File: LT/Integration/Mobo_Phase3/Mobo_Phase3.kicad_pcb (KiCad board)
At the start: 4 copper layers, 90.2 x 95.9 mm, 39 parts, among them J1 Bus, J2 Conn_Coaxial, J6 Conn_Coaxial, Q1 2N5486, U1 BAP64Q

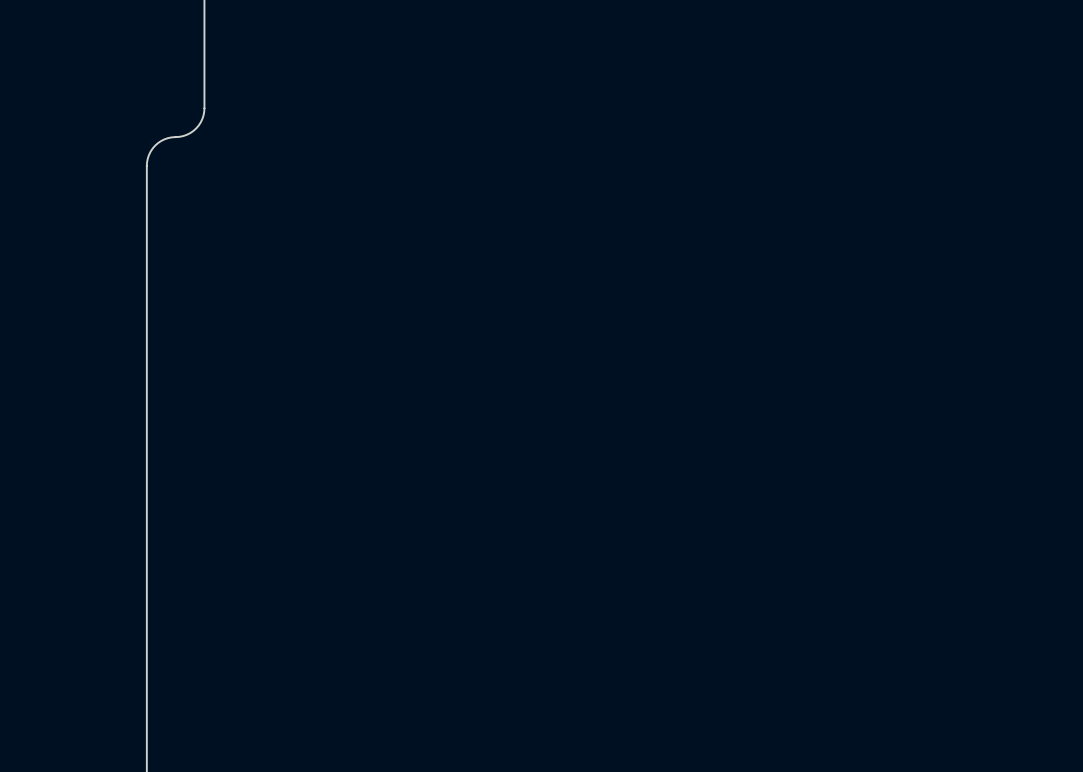
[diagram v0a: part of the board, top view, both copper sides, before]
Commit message: Finished 29.4 MHz BPF Schematic and Footprint association for Phase 3 of Mobo
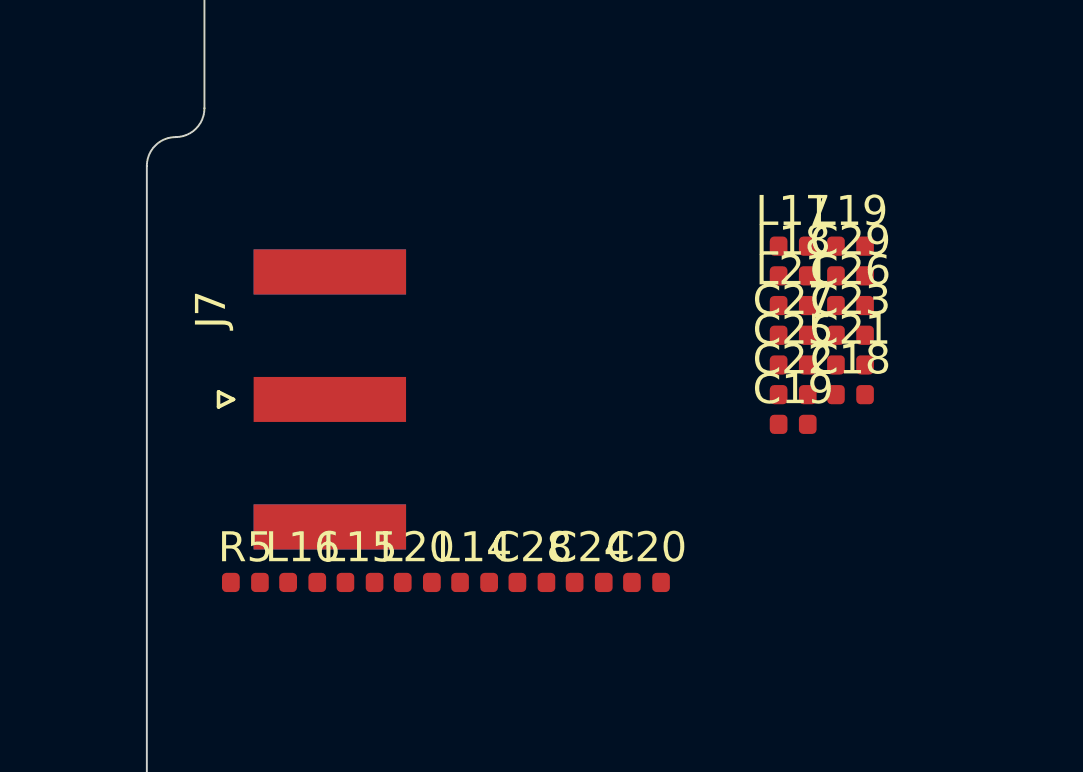
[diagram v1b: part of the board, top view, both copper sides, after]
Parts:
- added C18: No Connect, Capacitor_SMD:C_0402_1005Metric, F.Cu at (151.9, 103.2)
- added C19: 560pF, Capacitor_SMD:C_0402_1005Metric, F.Cu at (150.0, 104.2)
- added C20: 56 pF, Capacitor_SMD:C_0402_1005Metric, F.Cu at (145.1, 109.5)
- added C21: No Connect, Capacitor_SMD:C_0402_1005Metric, F.Cu at (151.9, 102.2)
- added C22: 18pF, Capacitor_SMD:C_0402_1005Metric, F.Cu at (150.0, 103.2)
- added C23: No Connect, Capacitor_SMD:C_0402_1005Metric, F.Cu at (151.9, 101.3)
- added C24: 43pF, Capacitor_SMD:C_0402_1005Metric, F.Cu at (143.2, 109.5)
- added C25: No Connect, Capacitor_SMD:C_0402_1005Metric, F.Cu at (150.0, 102.2)
- added C26: 560pF, Capacitor_SMD:C_0402_1005Metric, F.Cu at (151.9, 100.3)
- added C27: 56pF, Capacitor_SMD:C_0402_1005Metric, F.Cu at (150.0, 101.3)
- added C28: No Connect, Capacitor_SMD:C_0402_1005Metric, F.Cu at (141.3, 109.5)
- added C29: No Connect, Capacitor_SMD:C_0402_1005Metric, F.Cu at (151.9, 99.3)
- added J7: Conn_Coaxial, Connector_Coaxial:SMA_Amphenol_132289_EdgeMount, F.Cu at (134.6, 103.4)
- added L14: 47nH, Inductor_SMD:L_0402_1005Metric, F.Cu at (139.4, 109.5)
- added L15: 680nH, Inductor_SMD:L_0402_1005Metric, F.Cu at (135.6, 109.5)
- added L16: No Connect, Inductor_SMD:L_0402_1005Metric, F.Cu at (133.7, 109.5)
- added L17: 6.8nH, Inductor_SMD:L_0402_1005Metric, F.Cu at (150.0, 98.3)
- added L18: 1.5uH, Inductor_SMD:L_0402_1005Metric, F.Cu at (150.0, 99.3)
- added L19: No Connect, Inductor_SMD:L_0402_1005Metric, F.Cu at (151.9, 98.3)
- added L20: 72nH, Inductor_SMD:L_0402_1005Metric, F.Cu at (137.5, 109.5)
- added L21: 47nH, Inductor_SMD:L_0402_1005Metric, F.Cu at (150.0, 100.3)
- added R5: 0 Ohms, Resistor_SMD:R_0402_1005Metric, F.Cu at (131.8, 109.5)
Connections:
- C15 pad 2: (no net) -> /Low Noise Amplifier/Image_Reject_Out
- J1 pad 1: (no net) -> Net-(J1-Pad1)
- J1 pad 10: (no net) -> Net-(J1-Pad10)
- J1 pad 100: (no net) -> Net-(J1-Pad100)
- J1 pad 101: (no net) -> Net-(J1-Pad101)
- J1 pad 102: (no net) -> Net-(J1-Pad102)
- J1 pad 103: (no net) -> Net-(J1-Pad103)
- J1 pad 104: (no net) -> Net-(J1-Pad104)
- J1 pad 105: (no net) -> Net-(J1-Pad105)
- J1 pad 106: (no net) -> Net-(J1-Pad106)
- J1 pad 107: (no net) -> Net-(J1-Pad107)
- J1 pad 108: (no net) -> Net-(J1-Pad108)
- J1 pad 109: (no net) -> Net-(J1-Pad109)
- J1 pad 11: (no net) -> Net-(J1-Pad11)
- J1 pad 110: (no net) -> Net-(J1-Pad110)
- J1 pad 111: (no net) -> Net-(J1-Pad111)
- J1 pad 112: (no net) -> Net-(J1-Pad112)
- J1 pad 113: (no net) -> Net-(J1-Pad113)
- J1 pad 114: (no net) -> Net-(J1-Pad114)
- J1 pad 115: (no net) -> Net-(J1-Pad115)
- J1 pad 116: (no net) -> Net-(J1-Pad116)
- J1 pad 117: (no net) -> Net-(J1-Pad117)
- J1 pad 118: (no net) -> Net-(J1-Pad118)
- J1 pad 119: (no net) -> Net-(J1-Pad119)
- J1 pad 12: (no net) -> Net-(J1-Pad12)
- J1 pad 120: (no net) -> Net-(J1-Pad120)
- J1 pad 13: (no net) -> Net-(J1-Pad13)
- J1 pad 14: (no net) -> Net-(J1-Pad14)
- J1 pad 15: (no net) -> Net-(J1-Pad15)
- J1 pad 16: (no net) -> Net-(J1-Pad16)
- J1 pad 17: (no net) -> Net-(J1-Pad17)
- J1 pad 18: (no net) -> Net-(J1-Pad18)
- J1 pad 19: (no net) -> Net-(J1-Pad19)
- J1 pad 2: (no net) -> Net-(J1-Pad2)
- J1 pad 20: (no net) -> Net-(J1-Pad20)
- J1 pad 21: (no net) -> Net-(J1-Pad21)
- J1 pad 22: (no net) -> Net-(J1-Pad22)
- J1 pad 23: (no net) -> Net-(J1-Pad23)
- J1 pad 24: (no net) -> Net-(J1-Pad24)
- J1 pad 25: (no net) -> Net-(J1-Pad25)
- J1 pad 26: (no net) -> Net-(J1-Pad26)
- J1 pad 27: (no net) -> Net-(J1-Pad27)
- J1 pad 28: (no net) -> Net-(J1-Pad28)
- J1 pad 29: (no net) -> Net-(J1-Pad29)
- J1 pad 3: (no net) -> Net-(J1-Pad3)
- J1 pad 30: (no net) -> Net-(J1-Pad30)
- J1 pad 31: (no net) -> Net-(J1-Pad31)
- J1 pad 32: (no net) -> Net-(J1-Pad32)
- J1 pad 33: (no net) -> Net-(J1-Pad33)
- J1 pad 34: (no net) -> Net-(J1-Pad34)
- J1 pad 35: (no net) -> Net-(J1-Pad35)
- J1 pad 36: (no net) -> Net-(J1-Pad36)
- J1 pad 37: (no net) -> Net-(J1-Pad37)
- J1 pad 38: (no net) -> Net-(J1-Pad38)
- J1 pad 39: (no net) -> Net-(J1-Pad39)
- J1 pad 4: (no net) -> Net-(J1-Pad4)
- J1 pad 40: (no net) -> Net-(J1-Pad40)
- J1 pad 41: (no net) -> Net-(J1-Pad41)
- J1 pad 42: (no net) -> Net-(J1-Pad42)
- J1 pad 43: (no net) -> Net-(J1-Pad43)
- J1 pad 44: (no net) -> Net-(J1-Pad44)
- J1 pad 45: (no net) -> Net-(J1-Pad45)
- J1 pad 46: (no net) -> Net-(J1-Pad46)
- J1 pad 47: (no net) -> Net-(J1-Pad47)
- J1 pad 48: (no net) -> Net-(J1-Pad48)
- J1 pad 49: (no net) -> Net-(J1-Pad49)
- J1 pad 5: (no net) -> Net-(J1-Pad5)
- J1 pad 50: (no net) -> Net-(J1-Pad50)
- J1 pad 51: (no net) -> Net-(J1-Pad51)
- J1 pad 52: (no net) -> Net-(J1-Pad52)
- J1 pad 53: (no net) -> Net-(J1-Pad53)
- J1 pad 54: (no net) -> Net-(J1-Pad54)
- J1 pad 55: (no net) -> Net-(J1-Pad55)
- J1 pad 56: (no net) -> Net-(J1-Pad56)
- J1 pad 57: (no net) -> Net-(J1-Pad57)
- J1 pad 58: (no net) -> Net-(J1-Pad58)
- J1 pad 59: (no net) -> Net-(J1-Pad59)
- J1 pad 6: (no net) -> Net-(J1-Pad6)
- J1 pad 60: (no net) -> Net-(J1-Pad60)
- J1 pad 61: (no net) -> Net-(J1-Pad61)
- J1 pad 62: (no net) -> Net-(J1-Pad62)
- J1 pad 63: (no net) -> Net-(J1-Pad63)
- J1 pad 64: (no net) -> Net-(J1-Pad64)
- J1 pad 65: (no net) -> Net-(J1-Pad65)
- J1 pad 66: (no net) -> Net-(J1-Pad66)
- J1 pad 67: (no net) -> Net-(J1-Pad67)
- J1 pad 68: (no net) -> Net-(J1-Pad68)
- J1 pad 69: (no net) -> Net-(J1-Pad69)
- J1 pad 7: (no net) -> Net-(J1-Pad7)
- J1 pad 70: (no net) -> Net-(J1-Pad70)
- J1 pad 71: (no net) -> Net-(J1-Pad71)
- J1 pad 72: (no net) -> Net-(J1-Pad72)
- J1 pad 73: (no net) -> Net-(J1-Pad73)
- J1 pad 74: (no net) -> Net-(J1-Pad74)
- J1 pad 75: (no net) -> Net-(J1-Pad75)
- J1 pad 76: (no net) -> Net-(J1-Pad76)
- J1 pad 77: (no net) -> Net-(J1-Pad77)
- J1 pad 78: (no net) -> Net-(J1-Pad78)
- J1 pad 79: (no net) -> Net-(J1-Pad79)
- J1 pad 8: (no net) -> Net-(J1-Pad8)
- J1 pad 80: (no net) -> Net-(J1-Pad80)
- J1 pad 81: (no net) -> Net-(J1-Pad81)
- J1 pad 82: (no net) -> Net-(J1-Pad82)
- J1 pad 83: (no net) -> Net-(J1-Pad83)
- J1 pad 84: (no net) -> Net-(J1-Pad84)
- J1 pad 85: (no net) -> Net-(J1-Pad85)
- J1 pad 86: (no net) -> Net-(J1-Pad86)
- J1 pad 87: (no net) -> Net-(J1-Pad87)
- J1 pad 88: (no net) -> Net-(J1-Pad88)
- J1 pad 89: (no net) -> Net-(J1-Pad89)
- J1 pad 9: (no net) -> Net-(J1-Pad9)
- J1 pad 90: (no net) -> Net-(J1-Pad90)
- J1 pad 91: (no net) -> Net-(J1-Pad91)
- J1 pad 92: (no net) -> Net-(J1-Pad92)
- J1 pad 93: (no net) -> Net-(J1-Pad93)
- J1 pad 94: (no net) -> Net-(J1-Pad94)
- J1 pad 95: (no net) -> Net-(J1-Pad95)
- J1 pad 96: (no net) -> Net-(J1-Pad96)
- J1 pad 97: (no net) -> Net-(J1-Pad97)
- J1 pad 98: (no net) -> Net-(J1-Pad98)
- J1 pad 99: (no net) -> Net-(J1-Pad99)
- L12 pad 3: GND -> (no net)
- L13 pad 1: Net-(C17-Pad2) -> +8V
- L13 pad 3: +8V -> (no net)
- Q1 pad 2: GND -> Net-(C15-Pad1)
- Q1 pad 3: Net-(C15-Pad1) -> GND

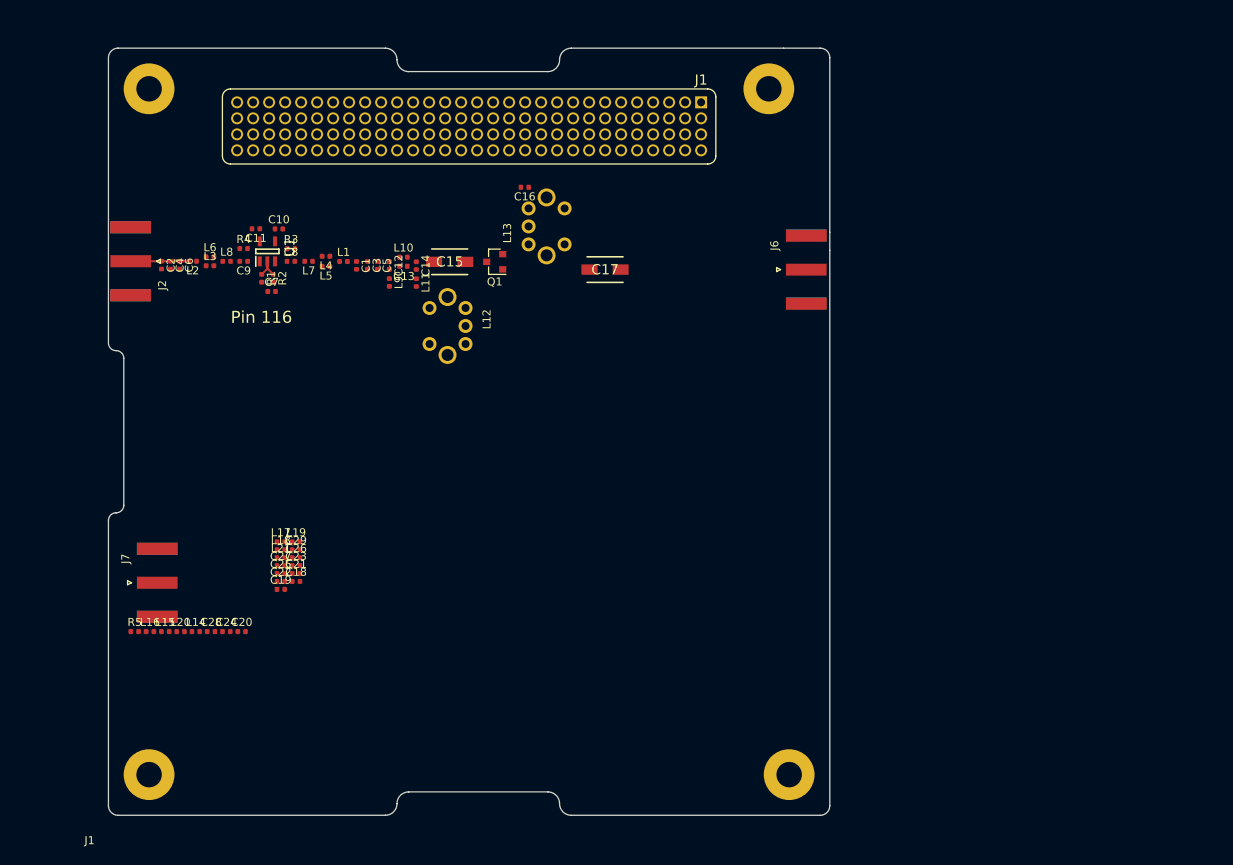
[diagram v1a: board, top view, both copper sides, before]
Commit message: Finished the preliminary layout of the receiving stage for MoBo Phase 3
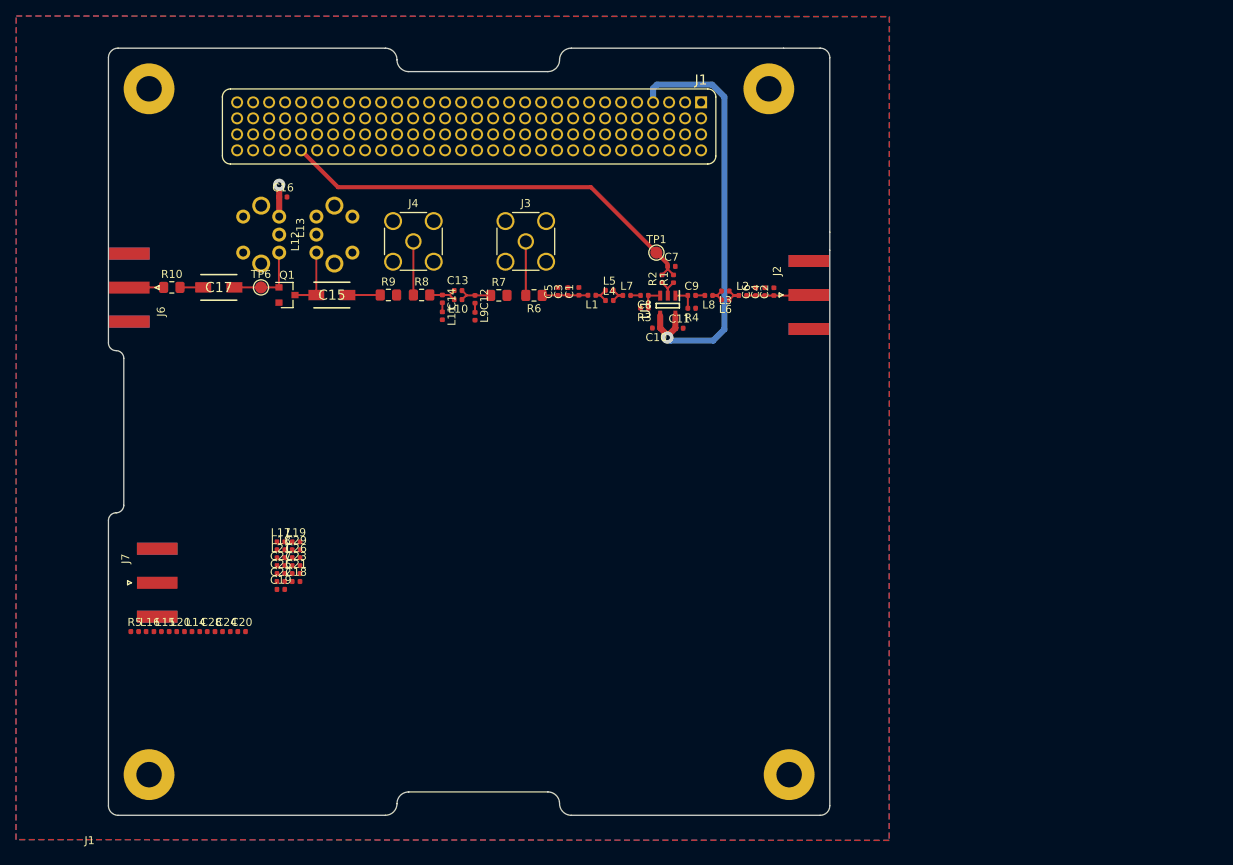
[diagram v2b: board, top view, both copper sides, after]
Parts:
- added J3: Conn_Coaxial, Connector_Coaxial:SMA_Amphenol_132291_Vertical, F.Cu at (180.7, 60.7)
- added J4: Conn_Coaxial, Connector_Coaxial:SMA_Amphenol_132291_Vertical, F.Cu at (166.6, 60.7)
- added R10: 0, Resistor_SMD:R_0805_2012Metric_Pad1.15x1.40mm_HandSolder, F.Cu at (136.4, 66.5)
- added R6: 0, Resistor_SMD:R_0805_2012Metric_Pad1.15x1.40mm_HandSolder, F.Cu at (181.7, 67.5)
- added R7: 0, Resistor_SMD:R_0805_2012Metric_Pad1.15x1.40mm_HandSolder, F.Cu at (177.3, 67.5)
- added R8: 0, Resistor_SMD:R_0805_2012Metric_Pad1.15x1.40mm_HandSolder, F.Cu at (167.6, 67.4)
- added R9: 0, Resistor_SMD:R_0805_2012Metric_Pad1.15x1.40mm_HandSolder, F.Cu at (163.5, 67.4)
- added TP1: TestPoint_Probe, TestPoint:TestPoint_Pad_D1.5mm, F.Cu at (197.0, 62.1)
- added TP6: TestPoint_Probe, TestPoint:TestPoint_Pad_D1.5mm, F.Cu at (147.6, 66.5)
- moved J2 84.9 mm to (216.0, 67.4), turned to 0 degrees
- moved J6 84.6 mm to (131.1, 66.5), turned to 180 degrees
- moved C2 76.6 mm to (211.7, 67.0), turned to 90 degrees
- moved C4 74.4 mm to (210.5, 67.0), turned to 90 degrees
- moved C6 72.1 mm to (209.4, 67.0), turned to 90 degrees
- moved L2 68.9 mm to (207.8, 67.5), turned to 0 degrees
- moved L6 64.6 mm to (205.6, 68.0), turned to 180 degrees
- moved L3 64.5 mm to (205.6, 66.9), turned to 180 degrees
- moved L8 60.4 mm to (203.5, 67.5), turned to 180 degrees
- moved R4 56.5 mm to (201.4, 69.1), turned to 180 degrees
- moved C9 56.2 mm to (201.4, 67.5), turned to 0 degrees
- moved C11 54.4 mm to (199.8, 71.6), turned to 0 degrees
- moved R1 51.5 mm to (199.1, 65.4), turned to 90 degrees
- moved U1 50.5 mm to (198.4, 68.8), turned to 270 degrees
- moved C7 50.1 mm to (198.9, 63.9)
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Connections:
- net /Image Reject Filter/Image_Reject_Out renamed Net-(C13-Pad1)
- net /Image Reject Filter/Variable_Attenuator_Out renamed Net-(C12-Pad1)
- net /Variable Attenuator/Variable_Attenuator_Out renamed Net-(C1-Pad1)
- C15 pad 2: /Low Noise Amplifier/Image_Reject_Out -> Net-(C15-Pad2)
- C17 pad 1: /Low Noise Amplifier/LNAout -> Net-(C17-Pad1)
- J1 pad 1: Net-(J1-Pad1) -> (no net)
- J1 pad 10: Net-(J1-Pad10) -> (no net)
- J1 pad 100: Net-(J1-Pad100) -> (no net)
- J1 pad 101: Net-(J1-Pad101) -> (no net)
- J1 pad 102: Net-(J1-Pad102) -> (no net)
- J1 pad 103: Net-(J1-Pad103) -> (no net)
- J1 pad 104: Net-(J1-Pad104) -> (no net)
- J1 pad 105: Net-(J1-Pad105) -> (no net)
- J1 pad 106: Net-(J1-Pad106) -> (no net)
- J1 pad 107: Net-(J1-Pad107) -> (no net)
- J1 pad 108: Net-(J1-Pad108) -> (no net)
- J1 pad 109: Net-(J1-Pad109) -> (no net)
- J1 pad 11: Net-(J1-Pad11) -> (no net)
- J1 pad 110: Net-(J1-Pad110) -> (no net)
- J1 pad 111: Net-(J1-Pad111) -> (no net)
- J1 pad 112: Net-(J1-Pad112) -> (no net)
- J1 pad 113: Net-(J1-Pad113) -> (no net)
- J1 pad 114: Net-(J1-Pad114) -> (no net)
- J1 pad 115: Net-(J1-Pad115) -> (no net)
- J1 pad 116: Net-(J1-Pad116) -> /Variable Attenuator/Control_Voltage_From_MicroController
- J1 pad 117: Net-(J1-Pad117) -> (no net)
- J1 pad 118: Net-(J1-Pad118) -> (no net)
- J1 pad 119: Net-(J1-Pad119) -> (no net)
- J1 pad 12: Net-(J1-Pad12) -> (no net)
- J1 pad 120: Net-(J1-Pad120) -> (no net)
- J1 pad 13: Net-(J1-Pad13) -> (no net)
- J1 pad 14: Net-(J1-Pad14) -> (no net)
- J1 pad 15: Net-(J1-Pad15) -> (no net)
- J1 pad 16: Net-(J1-Pad16) -> (no net)
- J1 pad 17: Net-(J1-Pad17) -> (no net)
- J1 pad 18: Net-(J1-Pad18) -> (no net)
- J1 pad 19: Net-(J1-Pad19) -> (no net)
- J1 pad 2: Net-(J1-Pad2) -> (no net)
- J1 pad 20: Net-(J1-Pad20) -> (no net)
- J1 pad 21: Net-(J1-Pad21) -> (no net)
- J1 pad 22: Net-(J1-Pad22) -> (no net)
- J1 pad 23: Net-(J1-Pad23) -> (no net)
- J1 pad 24: Net-(J1-Pad24) -> (no net)
- J1 pad 25: Net-(J1-Pad25) -> (no net)
- J1 pad 26: Net-(J1-Pad26) -> (no net)
- J1 pad 27: Net-(J1-Pad27) -> (no net)
- J1 pad 28: Net-(J1-Pad28) -> (no net)
- J1 pad 29: Net-(J1-Pad29) -> (no net)
- J1 pad 3: Net-(J1-Pad3) -> (no net)
- J1 pad 30: Net-(J1-Pad30) -> (no net)
- J1 pad 31: Net-(J1-Pad31) -> (no net)
- J1 pad 32: Net-(J1-Pad32) -> (no net)
- J1 pad 33: Net-(J1-Pad33) -> (no net)
- J1 pad 34: Net-(J1-Pad34) -> (no net)
- J1 pad 35: Net-(J1-Pad35) -> (no net)
- J1 pad 36: Net-(J1-Pad36) -> (no net)
- J1 pad 37: Net-(J1-Pad37) -> (no net)
- J1 pad 38: Net-(J1-Pad38) -> (no net)
- J1 pad 39: Net-(J1-Pad39) -> (no net)
- J1 pad 4: Net-(J1-Pad4) -> +5V
- J1 pad 40: Net-(J1-Pad40) -> (no net)
- J1 pad 41: Net-(J1-Pad41) -> (no net)
- J1 pad 42: Net-(J1-Pad42) -> (no net)
- J1 pad 43: Net-(J1-Pad43) -> (no net)
- J1 pad 44: Net-(J1-Pad44) -> (no net)
- J1 pad 45: Net-(J1-Pad45) -> (no net)
- J1 pad 46: Net-(J1-Pad46) -> (no net)
- J1 pad 47: Net-(J1-Pad47) -> (no net)
- J1 pad 48: Net-(J1-Pad48) -> (no net)
- J1 pad 49: Net-(J1-Pad49) -> (no net)
- J1 pad 5: Net-(J1-Pad5) -> (no net)
- J1 pad 50: Net-(J1-Pad50) -> (no net)
- J1 pad 51: Net-(J1-Pad51) -> (no net)
- J1 pad 52: Net-(J1-Pad52) -> (no net)
- J1 pad 53: Net-(J1-Pad53) -> (no net)
- J1 pad 54: Net-(J1-Pad54) -> (no net)
- J1 pad 55: Net-(J1-Pad55) -> (no net)
- J1 pad 56: Net-(J1-Pad56) -> (no net)
- J1 pad 57: Net-(J1-Pad57) -> (no net)
- J1 pad 58: Net-(J1-Pad58) -> (no net)
- J1 pad 59: Net-(J1-Pad59) -> (no net)
- J1 pad 6: Net-(J1-Pad6) -> (no net)
- J1 pad 60: Net-(J1-Pad60) -> (no net)
- J1 pad 61: Net-(J1-Pad61) -> (no net)
- J1 pad 62: Net-(J1-Pad62) -> (no net)
- J1 pad 63: Net-(J1-Pad63) -> (no net)
- J1 pad 64: Net-(J1-Pad64) -> (no net)
- J1 pad 65: Net-(J1-Pad65) -> (no net)
- J1 pad 66: Net-(J1-Pad66) -> (no net)
- J1 pad 67: Net-(J1-Pad67) -> (no net)
- J1 pad 68: Net-(J1-Pad68) -> (no net)
- J1 pad 69: Net-(J1-Pad69) -> (no net)
- J1 pad 7: Net-(J1-Pad7) -> (no net)
- J1 pad 70: Net-(J1-Pad70) -> (no net)
- J1 pad 71: Net-(J1-Pad71) -> (no net)
- J1 pad 72: Net-(J1-Pad72) -> (no net)
- J1 pad 73: Net-(J1-Pad73) -> (no net)
- J1 pad 74: Net-(J1-Pad74) -> (no net)
- J1 pad 75: Net-(J1-Pad75) -> (no net)
- J1 pad 76: Net-(J1-Pad76) -> (no net)
- J1 pad 77: Net-(J1-Pad77) -> (no net)
- J1 pad 78: Net-(J1-Pad78) -> (no net)
- J1 pad 79: Net-(J1-Pad79) -> (no net)
- J1 pad 8: Net-(J1-Pad8) -> (no net)
- J1 pad 80: Net-(J1-Pad80) -> (no net)
- J1 pad 81: Net-(J1-Pad81) -> (no net)
- J1 pad 82: Net-(J1-Pad82) -> (no net)
- J1 pad 83: Net-(J1-Pad83) -> (no net)
- J1 pad 84: Net-(J1-Pad84) -> (no net)
- J1 pad 85: Net-(J1-Pad85) -> (no net)
- J1 pad 86: Net-(J1-Pad86) -> (no net)
- J1 pad 87: Net-(J1-Pad87) -> (no net)
- J1 pad 88: Net-(J1-Pad88) -> (no net)
- J1 pad 89: Net-(J1-Pad89) -> (no net)
- J1 pad 9: Net-(J1-Pad9) -> (no net)
- J1 pad 90: Net-(J1-Pad90) -> (no net)
- J1 pad 91: Net-(J1-Pad91) -> (no net)
- J1 pad 92: Net-(J1-Pad92) -> (no net)
- J1 pad 93: Net-(J1-Pad93) -> (no net)
- J1 pad 94: Net-(J1-Pad94) -> (no net)
- J1 pad 95: Net-(J1-Pad95) -> (no net)
- J1 pad 96: Net-(J1-Pad96) -> (no net)
- J1 pad 97: Net-(J1-Pad97) -> (no net)
- J1 pad 98: Net-(J1-Pad98) -> (no net)
- J1 pad 99: Net-(J1-Pad99) -> (no net)
- L12 pad 3: (no net) -> GND
- L13 pad 2: Net-(C17-Pad2) -> GND
- L13 pad 3: (no net) -> Net-(C17-Pad2)
- Q1 pad 2: Net-(C15-Pad1) -> GND
- Q1 pad 3: GND -> Net-(C15-Pad1)
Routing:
- net /Variable Attenuator/Control_Voltage_From_MicroController: track 0.00 -> 54.7 mm
- net +5V: track 0.00 -> 54.7 mm, vias 0 -> 1
- net Net-(C17-Pad2): track 0.00 -> 9.99 mm
- net Net-(C15-Pad1): track 0.00 -> 7.98 mm
- net /Image Reject Filter/Image_Reject_Out: track 0.00 -> 6.71 mm
- net /Variable Attenuator/Variable_Attenuator_Out: track 0.00 -> 6.68 mm
- net Net-(C1-Pad1): track 0.00 -> 5.73 mm
- net Net-(C12-Pad1): track 0.00 -> 4.63 mm
- net /Low Noise Amplifier/LNAout: track 0.00 -> 4.57 mm
- net Net-(C13-Pad1): track 0.00 -> 4.11 mm
- net Net-(C15-Pad2): track 0.00 -> 4.09 mm
- net +8V: track 0.00 -> 3.98 mm, vias 0 -> 1
- net Net-(C9-Pad1): track 0.00 -> 3.13 mm
- net Net-(C8-Pad1): track 0.00 -> 3.09 mm
- net Net-(L1-Pad1): track 0.00 -> 2.97 mm
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- added copper zone on In2.Cu, net +8V
- added copper zone on B.Cu, net GND
- added copper zone on F.Cu, net GND
- added copper zone on In1.Cu, net GND
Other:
- board text removed: "Pin 116"
